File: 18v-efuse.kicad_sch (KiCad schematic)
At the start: 24 parts, among them J6 Conn_01x02, J7 Conn_01x02, U3 TPS259470x, U5 TPS259470x

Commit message: schem: add usb pwr input with TPS259470x 5V 3A efuse
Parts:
- added C34: 1n, Capacitor_SMD:C_0402_1005Metric, symbol Device:C
- added D12: H5VU10U, GLCS:Diode_DFN1006, symbol GLCS:H5VU10U
- added D14: GREEN, LED_SMD:LED_0805_2012Metric, symbol Device:LED
- added J1: USB_C_Receptacle_USB2.0_14P, Connector_USB:USB_C_Receptacle_HRO_TYPE-C-31-M-12, symbol Connector:USB_C_Receptacle_USB2.0_14P
- added R13: 1k, Resistor_SMD:R_0402_1005Metric, symbol Device:R
- added R22: 10k, Resistor_SMD:R_0402_1005Metric, symbol Device:R
- added R23: 3k3, Resistor_SMD:R_0402_1005Metric, symbol Device:R
- added R24, R4, R6: 5k1, Resistor_SMD:R_0402_1005Metric, symbol Device:R
- added U7: TPS259470x, GLCS:Texas_RPW0010A_VQFN-HR-10_2x2mm_P0.5mm, symbol GLCS:TPS259470x
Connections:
- net +3V3: now also R24.2
- net GND: now also C34.2, D12.2 (A), J1.A1 (GND), J1.A12 (GND), J1.B1 (GND), J1.B12 (GND), J1.SH (SHIELD), R13.2, R23.1, R4.1, R6.1, U7.2 (OVLO), U7.8 (GND)
- net ILM: now also R13.1, U7.9 (ILM)
- new net: R22.1, R23.2, U7.1 (EN/UVLO)
- new net: J1.A5 (CC1), R4.2
- new net: C34.1, U7.7 (DVDT)
- new net: D14.1 (K), U7.4 (~{FLT})
- new net: D14.2 (A), R24.1
- new net: J1.B5 (CC2), R6.2
- new net +Vbus: D12.1 (K), J1.A4 (VBUS), J1.A9 (VBUS), J1.B4 (VBUS), J1.B9 (VBUS), R22.2, U7.5 (IN)
- no-connect marks 2 -> 8
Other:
- note added: "2x TPS259470x 18V 1A efuse"
- note added: "TPS259470x 5V 3A efuse"
- note added: "USB/ESP"
- note removed: "TPS259470x 1A efuse"
- moved on the sheet: C26, C27, C28, C29, C30, C31, C32, C33, D10, D11, J6, J7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

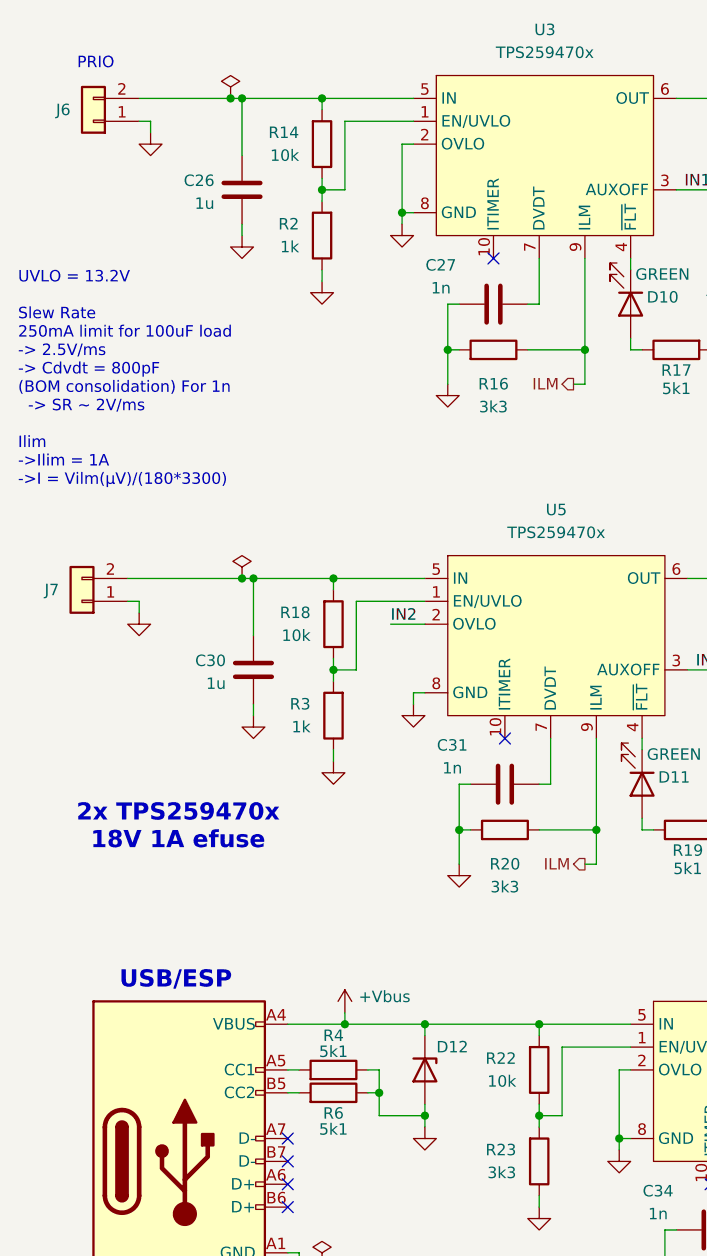
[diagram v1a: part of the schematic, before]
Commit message: schem: add power protection diodes
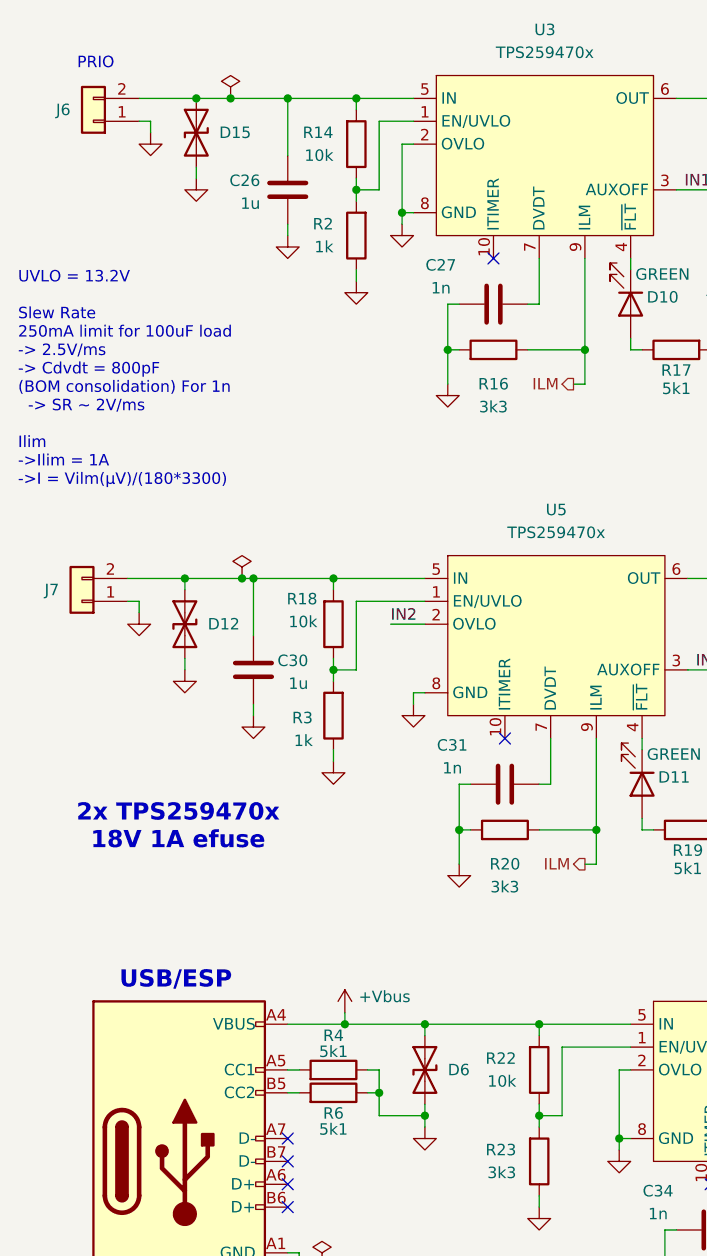
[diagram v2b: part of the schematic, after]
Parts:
- removed D12: H5VU10U, GLCS:Diode_DFN1006, symbol GLCS:H5VU10U
- added D12, D15: SMBJ6.0CA, Diode_SMD:D_SMA, symbol Device:D_TVS
- added D6: SMBJ6.0CA, Diode_SMD:D_SMB, symbol Device:D_TVS
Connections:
- net +Vbus: now also D6.1 (A1)
- net GND: now also D12.2 (A2), D15.2 (A2), D6.2 (A2)
- net at C26.2, J6.2 (Pin_2), R14.2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: now also D15.1 (A1)
- net at C30.2, J7.2 (Pin_2), R18.2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: now also D12.1 (A1)
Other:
- moved on the sheet: C26, R14, R2

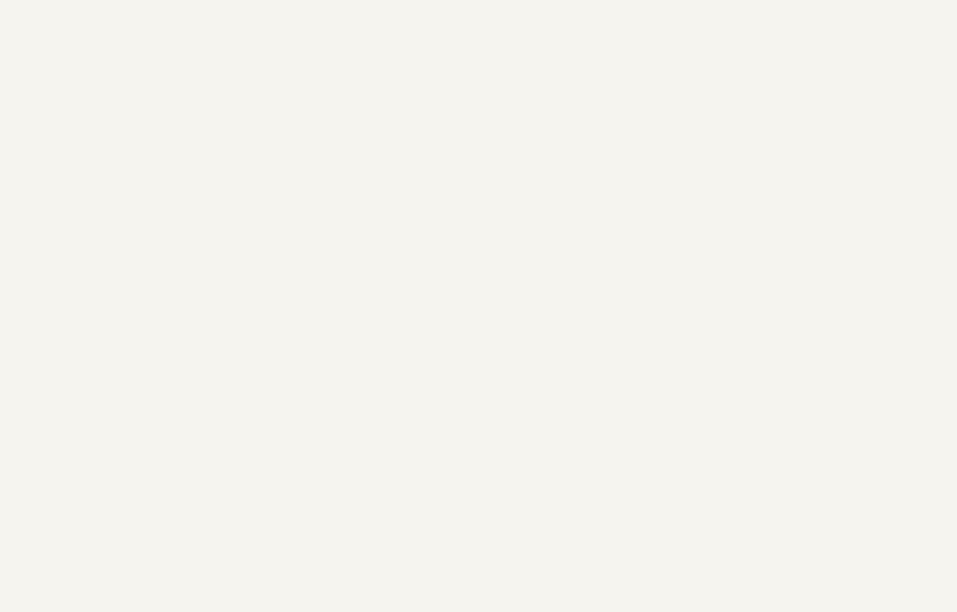
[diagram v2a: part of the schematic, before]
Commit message: schem: move smps to second page
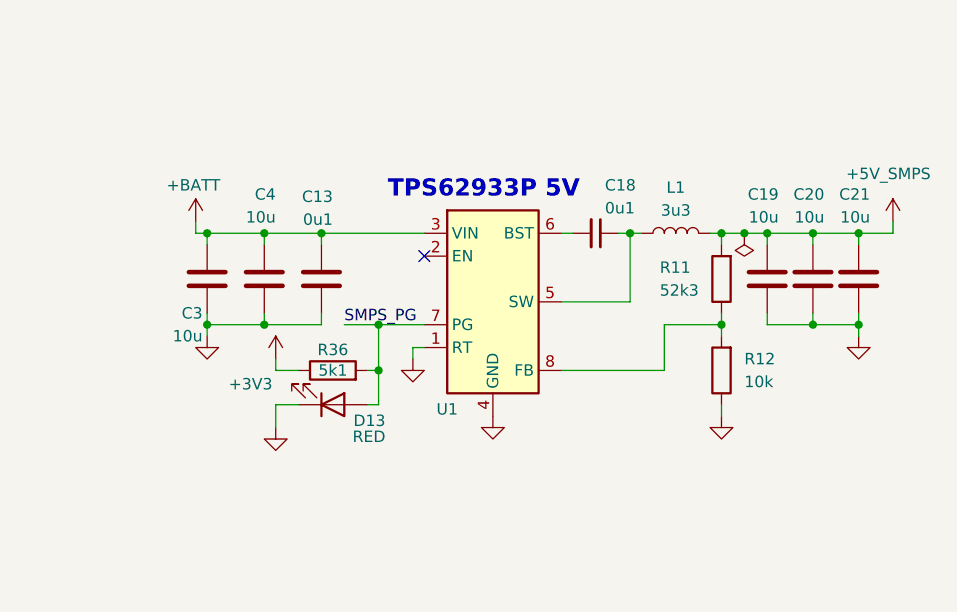
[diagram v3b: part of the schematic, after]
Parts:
- added C13: 0u1, Capacitor_SMD:C_0402_1005Metric, symbol Device:C
- added C18: 0u1, Capacitor_SMD:C_0402_1005Metric, symbol Device:C_Small
- added C19, C20, C21, C3, C4: 10u, Capacitor_SMD:C_0805_2012Metric, symbol Device:C
- added D13: RED, LED_SMD:LED_0805_2012Metric, symbol Device:LED
- added L1: 3u3, Inductor_SMD:L_Sunlord_MWSA0402S, symbol Device:L
- added R11: 52k3, Resistor_SMD:R_0402_1005Metric, symbol Device:R
- added R12: 10k, Resistor_SMD:R_0402_1005Metric, symbol Device:R
- added R36: 5k1, Resistor_SMD:R_0402_1005Metric, symbol Device:R
- added U1: TPS62933, Package_TO_SOT_SMD:SOT-583-8, symbol Regulator_Switching:TPS62933P
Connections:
- net +3V3: now also R36.1
- net +BATT: now also C13.1, C3.1, C4.1, U1.3 (VIN)
- net GND: now also C13.2, C19.2, C20.2, C21.2, C3.2, C4.2, D13.1 (K), R12.1, U1.1 (RT), U1.4 (GND)
- new net: C18.1, L1.1, U1.5 (SW)
- new net: R11.1, R12.2, U1.8 (FB)
- new net: C18.2, U1.6 (BST)
- new net +5V_SMPS: C19.1, C20.1, C21.1, L1.2, R11.2
- new net SMPS_PG: D13.2 (A), R36.2, U1.7 (PG)
- no-connect marks 8 -> 9
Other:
- note added: "TPS62933P 5V"

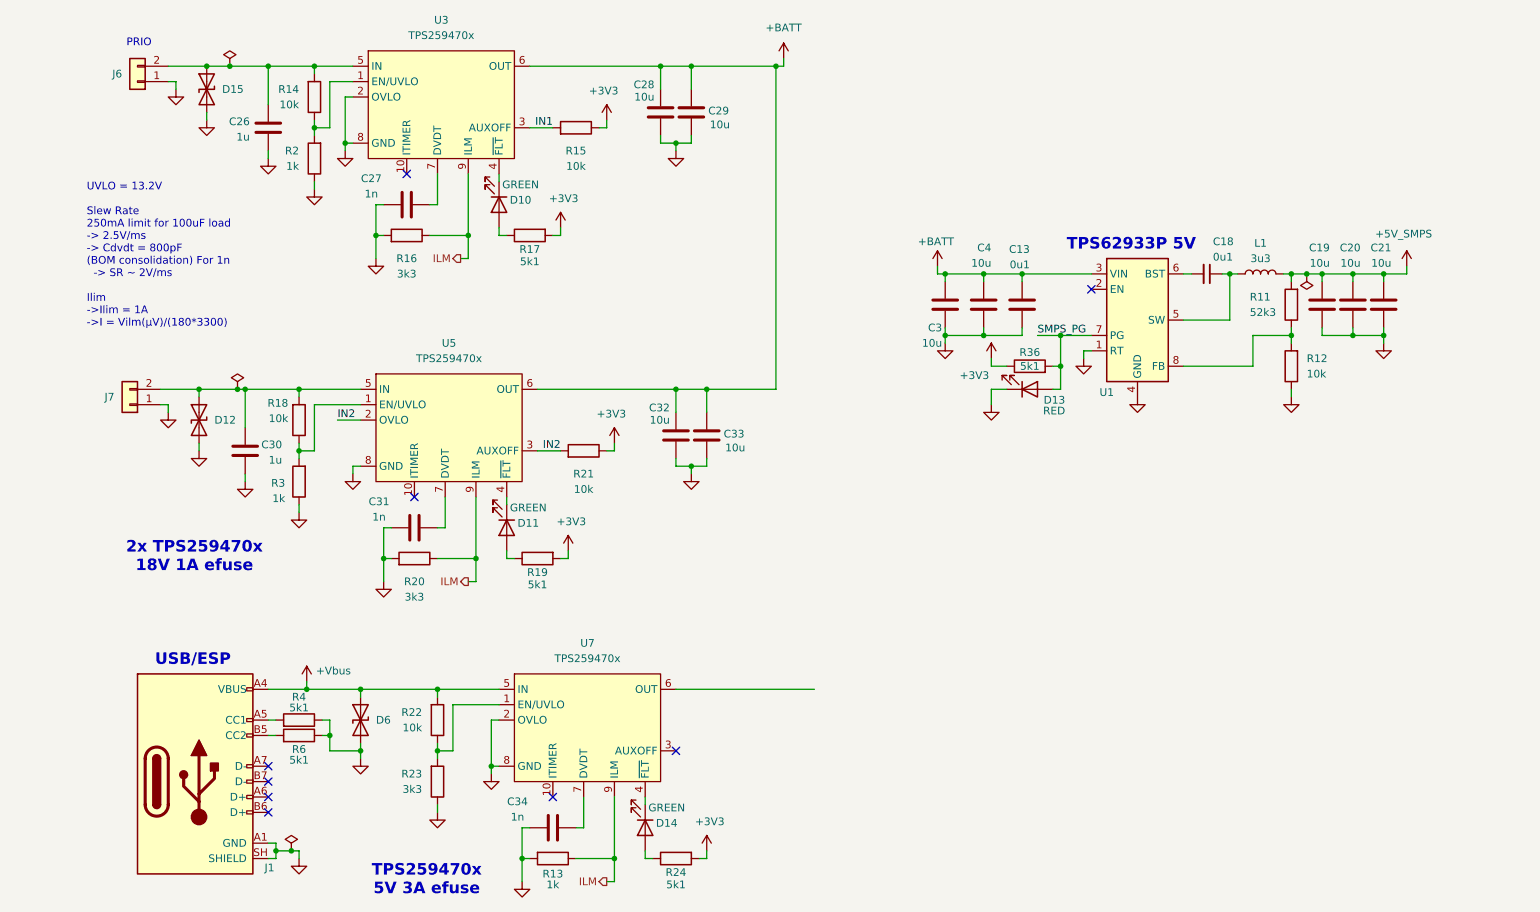
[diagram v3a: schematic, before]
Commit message: schem: add +5v efuses
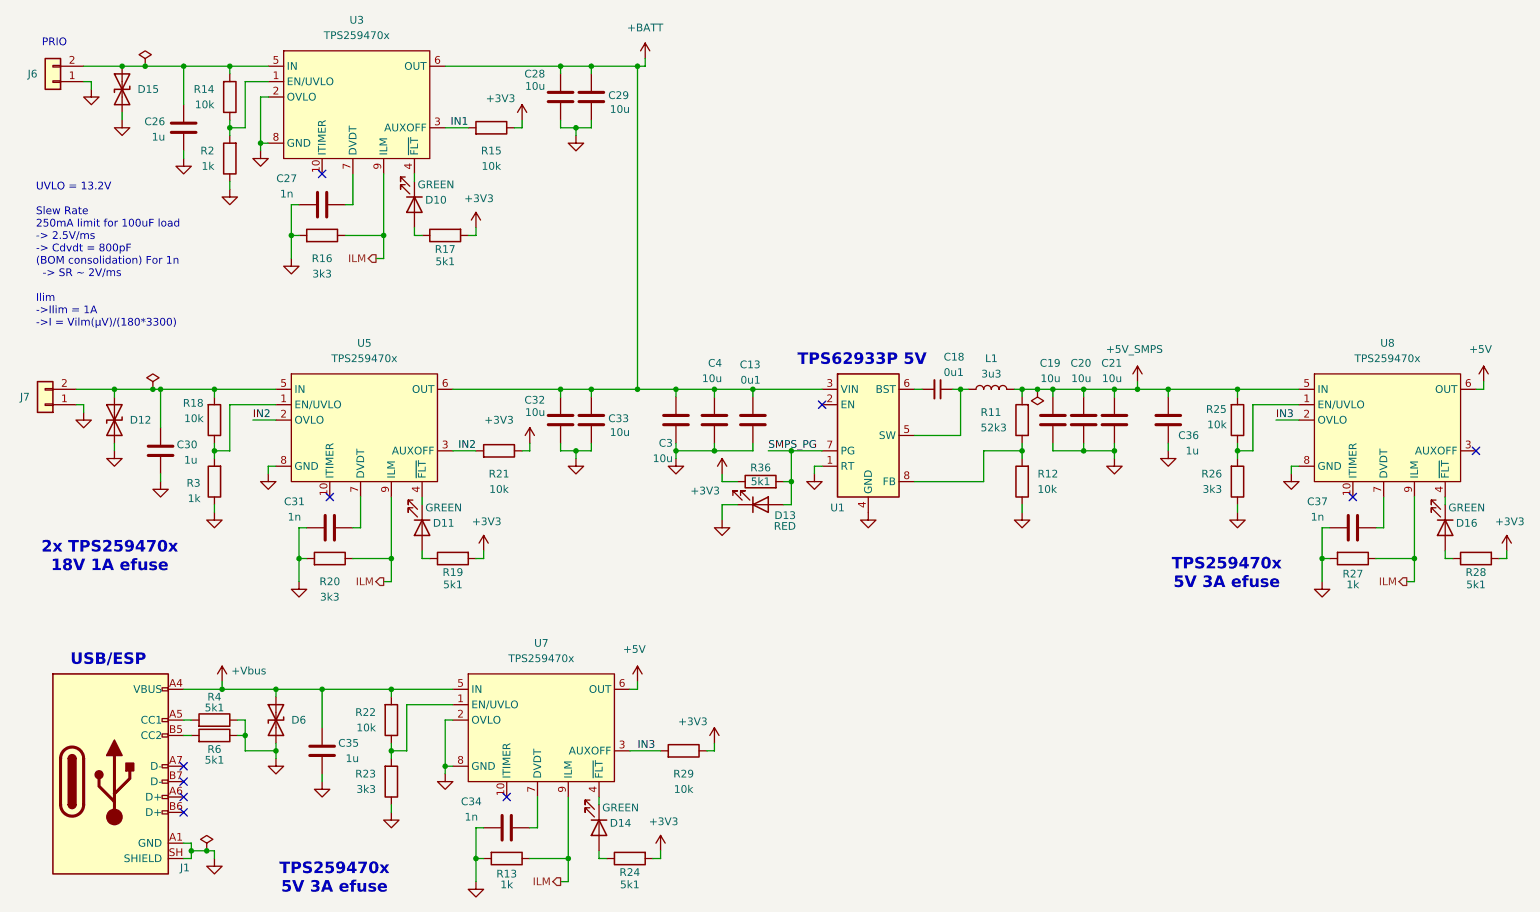
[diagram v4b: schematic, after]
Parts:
- added C35, C36: 1u, Capacitor_SMD:C_0402_1005Metric, symbol Device:C
- added C37: 1n, Capacitor_SMD:C_0402_1005Metric, symbol Device:C
- added D16: GREEN, LED_SMD:LED_0805_2012Metric, symbol Device:LED
- added R25, R29: 10k, Resistor_SMD:R_0402_1005Metric, symbol Device:R
- added R26: 3k3, Resistor_SMD:R_0402_1005Metric, symbol Device:R
- added R27: 1k, Resistor_SMD:R_0402_1005Metric, symbol Device:R
- added R28: 5k1, Resistor_SMD:R_0402_1005Metric, symbol Device:R
- added U8: TPS259470x, GLCS:Texas_RPW0010A_VQFN-HR-10_2x2mm_P0.5mm, symbol GLCS:TPS259470x
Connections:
- net +3V3: now also R28.2, R29.1
- net +5V_SMPS: now also C36.2, R25.2, U8.5 (IN)
- net +Vbus: now also C35.2
- net GND: now also C35.1, C36.1, C37.2, R26.1, R27.2, U8.8 (GND)
- net ILM: now also R27.1, U8.9 (ILM)
- net IN3: now reaches U7.3 (AUXOFF)
- net IN3: now also R29.2, U8.2 (OVLO)
- net +5V: now reaches U7.6 (OUT)
- net +5V: now also U8.6 (OUT)
- new net: C37.1, U8.7 (DVDT)
- new net: D16.1 (K), U8.4 (~{FLT})
- new net: D16.2 (A), R28.1
- new net: R25.1, R26.2, U8.1 (EN/UVLO)
- no-connect marks 9 -> 10
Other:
- moved on the sheet: C13, C18, C19, C20, C21, C26, C27, C28, C29, C3, C30, C31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
